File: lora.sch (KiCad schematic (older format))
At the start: 51 parts, among them J11 Conn_Coaxial, J2 Humidity, J3 Temp, J5 Temp, J6 VDD, J7 GPS, J8 SIM800, J9 I2C, Q1 AO3401A, Q2 AO3401A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

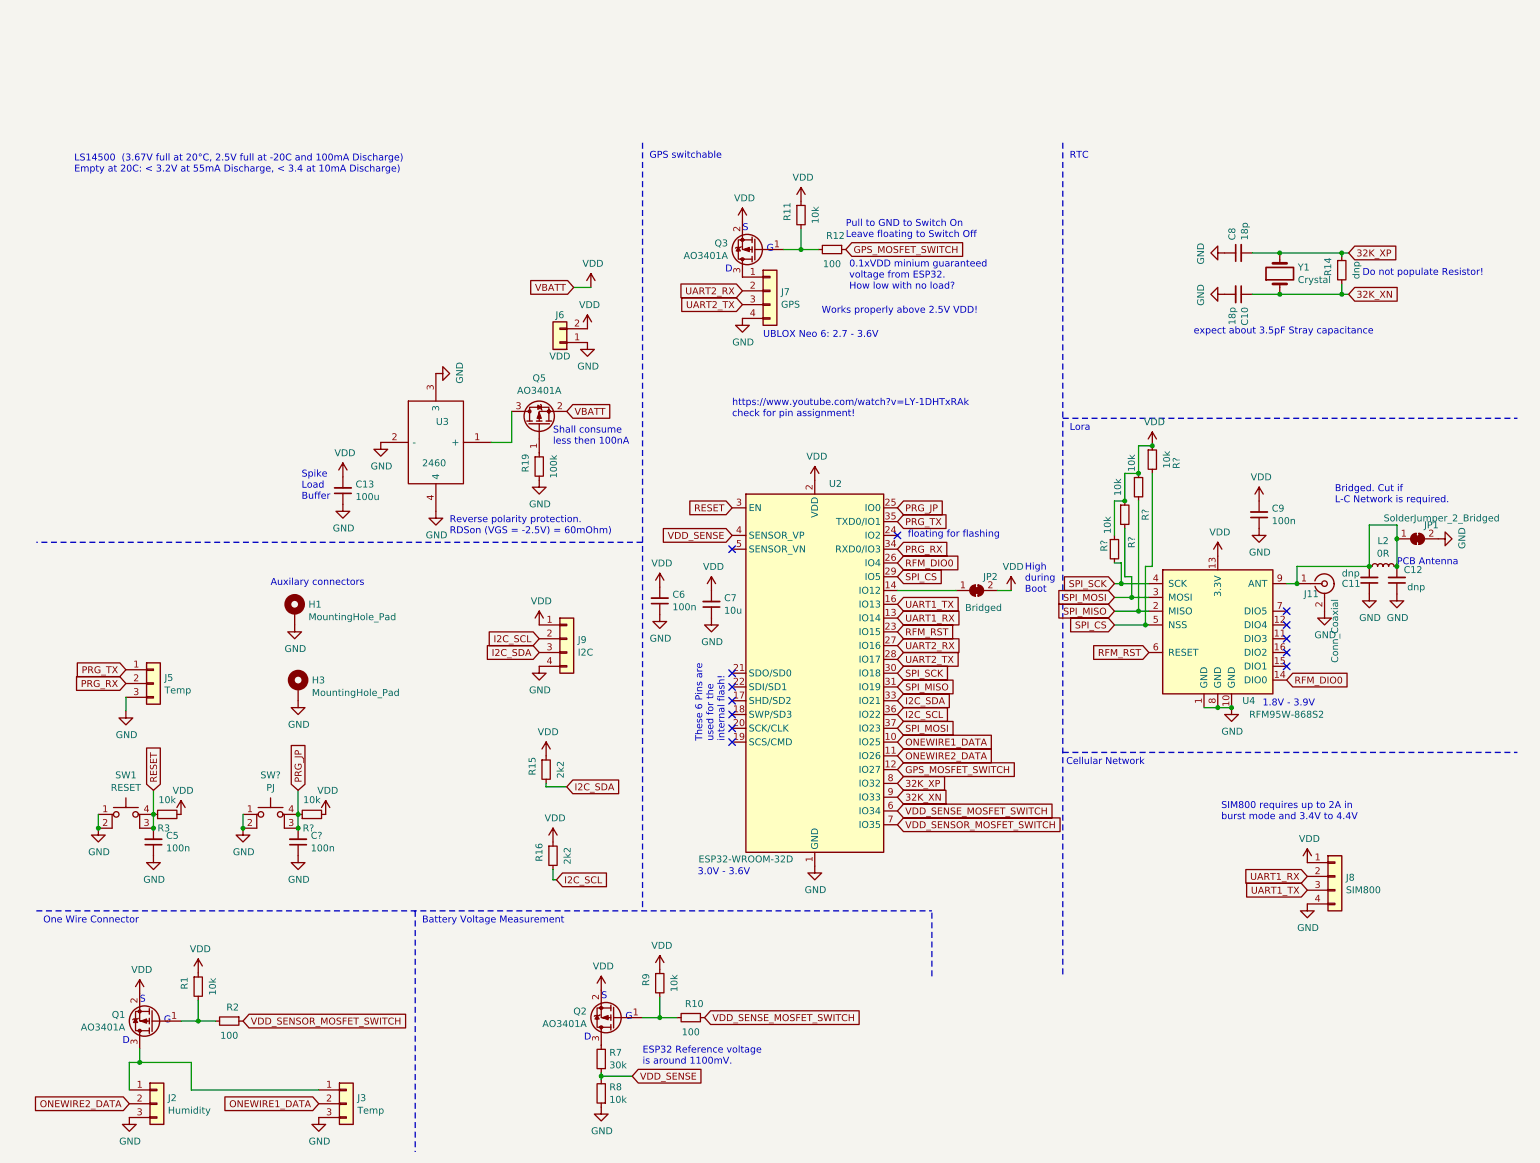
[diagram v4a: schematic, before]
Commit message: add onewire pullup
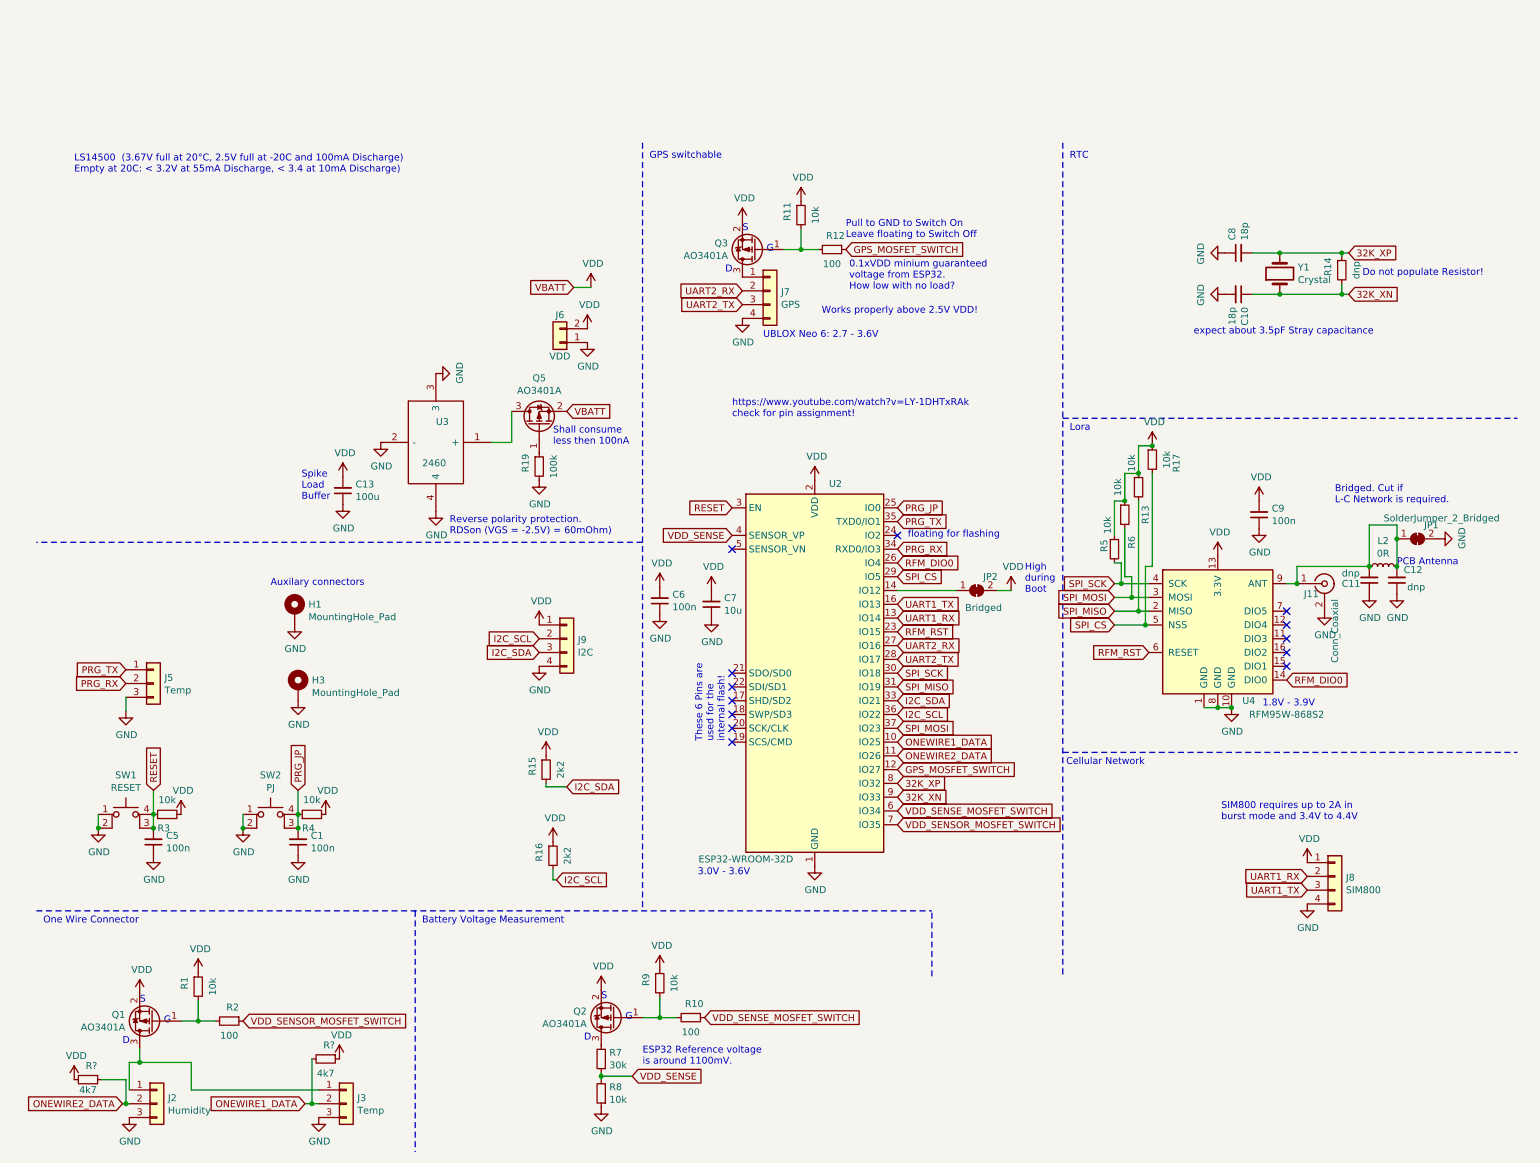
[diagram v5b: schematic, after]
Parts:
- added R? (x2): 4k7, Capacitor_SMD:C_0603_1608Metric, symbol Device:R_Small
- gave numbers to parts that had none: 7
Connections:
- net ONEWIRE1_DATA: now also R?.2
- net ONEWIRE2_DATA: now also R?.1
- net VDD: now also R?.1, R?.2
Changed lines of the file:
@@
 Text Notes 4875 7175 0    50   ~ 0
 ESP32 Reference voltage\nis around 1100mV. \n
-Text GLabel 1150 7450 0    50   Input ~ 0
+Text GLabel 1100 7450 0    50   Input ~ 0
 ONEWIRE2_DATA
 Text GLabel 9700 5800 0    50   Input ~ 0
@@
 	1    0    0    -1
 $EndComp
-Text GLabel 2525 7450 0    50   Input ~ 0
+Text GLabel 2425 7450 0    50   Input ~ 0
 ONEWIRE1_DATA
 $Comp
@@
 LS14500  (3.67V full at 20°C, 2.5V full at -20C and 100mA Discharge)\nEmpty at 20C: < 3.2V at 55mA Discharge, < 3.4 at 10mA Discharge)
 $Comp
-L Switch:SW_MEC_5E SW?
+L Switch:SW_MEC_5E SW2
 U 1 1 613DD3E9
 P 2175 5450
-F 0 "SW?" H 2175 5835 50  0000 C CNN
+F 0 "SW2" H 2175 5835 50  0000 C CNN
 F 1 "PJ" H 2175 5744 50  0000 C CNN
 F 2 "OWN_Parts_:TS-1187A-C-E-B" H 2175 5750 50  0001 C CNN
@@
 $EndComp
 $Comp
-L Device:R_Small R?
+L Device:R_Small R4
 U 1 1 613DD3F0
 P 2475 5350
-F 0 "R?" V 2375 5375 50  0000 C CNN
+F 0 "R4" V 2375 5375 50  0000 C CNN
 F 1 "10k" V 2580 5350 50  0000 C CNN
 F 2 "Capacitor_SMD:C_0603_1608Metric" H 2475 5350 50  0001 C CNN
@@
 $EndComp
 $Comp
-L power:VDD #PWR?
+L power:VDD #PWR0115
 U 1 1 613DD3F6
 P 2575 5350
-F 0 "#PWR?" H 2575 5200 50  0001 C CNN
+F 0 "#PWR0115" H 2575 5200 50  0001 C CNN
 F 1 "VDD" H 2590 5523 50  0000 C CNN
 F 2 "" H 2575 5350 50  0001 C CNN
@@
 $EndComp
 $Comp
-L power:GND #PWR?
+L power:GND #PWR0118
 U 1 1 613DD3FC
 P 1975 5450
-F 0 "#PWR?" H 1975 5200 50  0001 C CNN
+F 0 "#PWR0118" H 1975 5200 50  0001 C CNN
 F 1 "GND" H 1980 5277 50  0000 C CNN
 F 2 "" H 1975 5450 50  0001 C CNN
@@
 	2375 5350 2375 5175
 $Comp
-L Device:C_Small C?
+L Device:C_Small C1
 U 1 1 613DD409
 P 2375 5550
-F 0 "C?" H 2283 5504 50  0000 R CNN
+F 0 "C1" H 2283 5504 50  0000 R CNN
 F 1 "100n" H 2283 5595 50  0000 R CNN
 F 2 "Capacitor_SMD:C_0603_1608Metric" H 2375 5550 50  0001 C CNN
@@
 Connection ~ 2375 5450
 $Comp
-L power:GND #PWR?
+L power:GND #PWR0132
 U 1 1 613DD410
 P 2375 5650
-F 0 "#PWR?" H 2375 5400 50  0001 C CNN
+F 0 "#PWR0132" H 2375 5400 50  0001 C CNN
 F 1 "GND" H 2380 5477 50  0000 C CNN
 F 2 "" H 2375 5650 50  0001 C CNN
@@
 $EndComp
 $Comp
-L Device:R_Small R?
+L Device:R_Small R13
 U 1 1 613E1CFC
 P 8475 2975
-F 0 "R?" V 8525 2775 50  0000 C CNN
+F 0 "R13" V 8525 2775 50  0000 C CNN
 F 1 "10k" V 8425 3150 50  0000 C CNN
 F 2 "Capacitor_SMD:C_0603_1608Metric" H 8475 2975 50  0001 C CNN
@@
 $EndComp
 $Comp
-L Device:R_Small R?
+L Device:R_Small R17
 U 1 1 613E1FD9
 P 8575 2775
-F 0 "R?" V 8750 2750 50  0000 C CNN
+F 0 "R17" V 8750 2750 50  0000 C CNN
 F 1 "10k" V 8680 2775 50  0000 C CNN
 F 2 "Capacitor_SMD:C_0603_1608Metric" H 8575 2775 50  0001 C CNN
@@
 $EndComp
 $Comp
-L Device:R_Small R?
+L Device:R_Small R6
 U 1 1 613E1A6B
 P 8375 3175
-F 0 "R?" V 8425 2975 50  0000 C CNN
+F 0 "R6" V 8425 2975 50  0000 C CNN
 F 1 "10k" V 8325 3375 50  0000 C CNN
 F 2 "Capacitor_SMD:C_0603_1608Metric" H 8375 3175 50  0001 C CNN
@@
 $EndComp
 $Comp
-L Device:R_Small R?
+L Device:R_Small R5
 U 1 1 613E0914
 P 8300 3425
-F 0 "R?" V 8225 3450 50  0000 C CNN
+F 0 "R5" V 8225 3450 50  0000 C CNN
 F 1 "10k" V 8250 3600 50  0000 C CNN
 F 2 "Capacitor_SMD:C_0603_1608Metric" H 8300 3425 50  0001 C CNN
@@
 Connection ~ 8475 2875
 $Comp
-L power:VDD #PWR?
+L power:VDD #PWR0135
 U 1 1 613F2A9A
 P 8575 2675
-F 0 "#PWR?" H 8575 2525 50  0001 C CNN
+F 0 "#PWR0135" H 8575 2525 50  0001 C CNN
 F 1 "VDD" H 8590 2848 50  0000 C CNN
 F 2 "" H 8575 2675 50  0001 C CNN
@@
 Wire Wire Line
 	8350 3675 8550 3675
+$Comp
+L Device:R_Small R?
+U 1 1 614025B8
+P 2575 7125
+F 0 "R?" V 2475 7150 50  0000 C CNN
+F 1 "4k7" V 2680 7125 50  0000 C CNN
+F 2 "Capacitor_SMD:C_0603_1608Metric" H 2575 7125 50  0001 C CNN
+F 3 "~" H 2575 7125 50  0001 C CNN
+F 4 "C23162" H 2575 7125 50  0001 C CNN "LCSC"
+	1    2575 7125
+	0    1    1    0
+$EndComp
+$Comp
+L Device:R_Small R?
+U 1 1 61403C1F
+P 850 7275
+F 0 "R?" V 750 7300 50  0000 C CNN
+F 1 "4k7" V 925 7275 50  0000 C CNN
+F 2 "Capacitor_SMD:C_0603_1608Metric" H 850 7275 50  0001 C CNN
+F 3 "~" H 850 7275 50  0001 C CNN
+F 4 "C23162" H 850 7275 50  0001 C CNN "LCSC"
+	1    850  7275
+	0    1    1    0
+$EndComp
+$Comp
+L power:VDD #PWR?
+U 1 1 6140430D
+P 2675 7125
+F 0 "#PWR?" H 2675 6975 50  0001 C CNN
+F 1 "VDD" H 2690 7298 50  0000 C CNN
+F 2 "" H 2675 7125 50  0001 C CNN
+F 3 "" H 2675 7125 50  0001 C CNN
+	1    2675 7125
+	1    0    0    -1
+$EndComp
+$Comp
+L power:VDD #PWR?
+U 1 1 61405B69
+P 750 7275
+F 0 "#PWR?" H 750 7125 50  0001 C CNN
+F 1 "VDD" H 765 7448 50  0000 C CNN
+F 2 "" H 750 7275 50  0001 C CNN
+F 3 "" H 750 7275 50  0001 C CNN
+	1    750  7275
+	1    0    0    -1
+$EndComp
+Wire Wire Line
+	2425 7450 2475 7450
+Wire Wire Line
+	2475 7125 2475 7450
+Connection ~ 2475 7450
+Wire Wire Line
+	2475 7450 2525 7450
+Wire Wire Line
+	1150 7450 1125 7450
+Wire Wire Line
+	1125 7450 1125 7275
+Wire Wire Line
+	1125 7275 950  7275
+Connection ~ 1125 7450
+Wire Wire Line
+	1125 7450 1100 7450
 $EndSCHEMATC

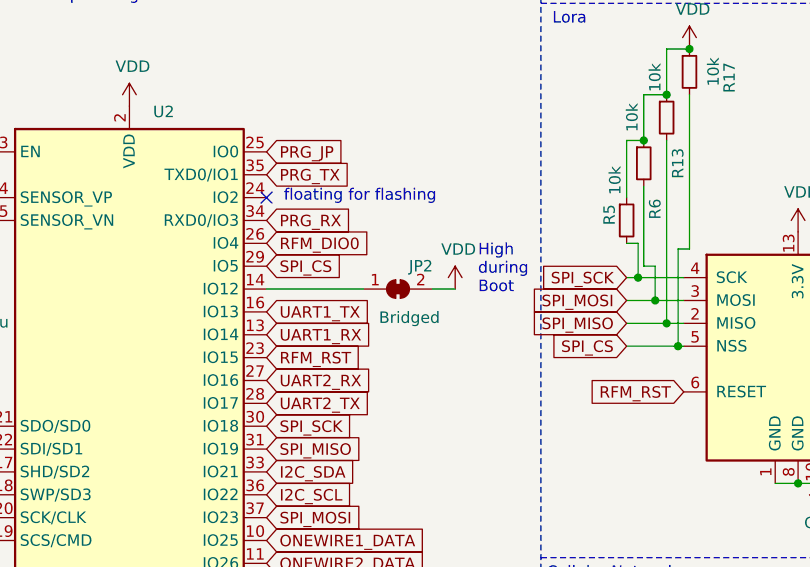
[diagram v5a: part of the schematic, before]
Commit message: remove JP2, add hints for StepUP DCDC
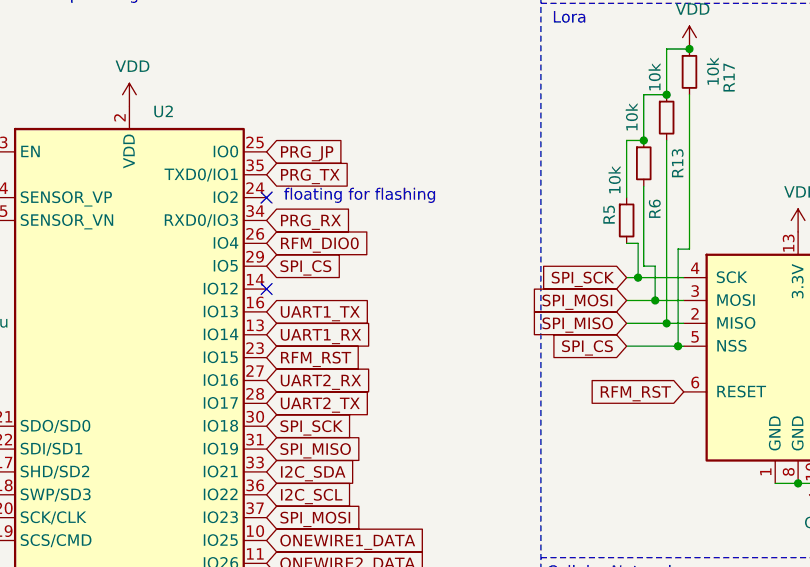
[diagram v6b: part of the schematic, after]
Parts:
- removed JP2: Bridged, Jumper:SolderJumper-2_P1.3mm_Bridged_Pad1.0x1.5mm, symbol Jumper:SolderJumper_2_Bridged
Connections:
- no-connect marks 13 -> 14
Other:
- note removed: "High \nduring \nBoot"
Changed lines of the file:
@@
 https://www.youtube.com/watch?v=LY-1DHTxRAk\ncheck for pin assignment!
 NoConn ~ 6725 3325
-Text Notes 7650 3750 0    50   ~ 0
-High \nduring \nBoot
 Text Notes 5475 4825 1    50   ~ 0
 These 6 Pins are\nused for the\ninternal flash!
 NoConn ~ 5525 4525
 NoConn ~ 5525 4625
-$Comp
-L power:VDD #PWR06
-U 1 1 5FD0859A
-P 7550 3725
-F 0 "#PWR06" H 7550 3575 50  0001 C CNN
-F 1 "VDD" H 7565 3898 50  0000 C CNN
-F 2 "" H 7550 3725 50  0001 C CNN
-F 3 "" H 7550 3725 50  0001 C CNN
-	1    7550 3725
-	1    0    0    -1
-$EndComp
-$Comp
-L Jumper:SolderJumper_2_Bridged JP2
-U 1 1 5FD08A69
-P 7300 3725
-F 0 "JP2" H 7400 3825 50  0000 C CNN
-F 1 "Bridged" H 7350 3600 50  0000 C CNN
-F 2 "Jumper:SolderJumper-2_P1.3mm_Bridged_Pad1.0x1.5mm" H 7300 3725 50  0001 C CNN
-F 3 "~" H 7300 3725 50  0001 C CNN
-	1    7300 3725
-	1    0    0    -1
-$EndComp
-Wire Wire Line
-	7150 3725 6725 3725
-Wire Wire Line
-	7550 3725 7450 3725
 Text Notes 6800 3350 0    50   ~ 0
 floating for flashing
@@
 Wire Wire Line
 	1125 7450 1100 7450
+NoConn ~ 6725 3725
 $EndSCHEMATC
